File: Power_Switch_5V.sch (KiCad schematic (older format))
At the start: 7 parts

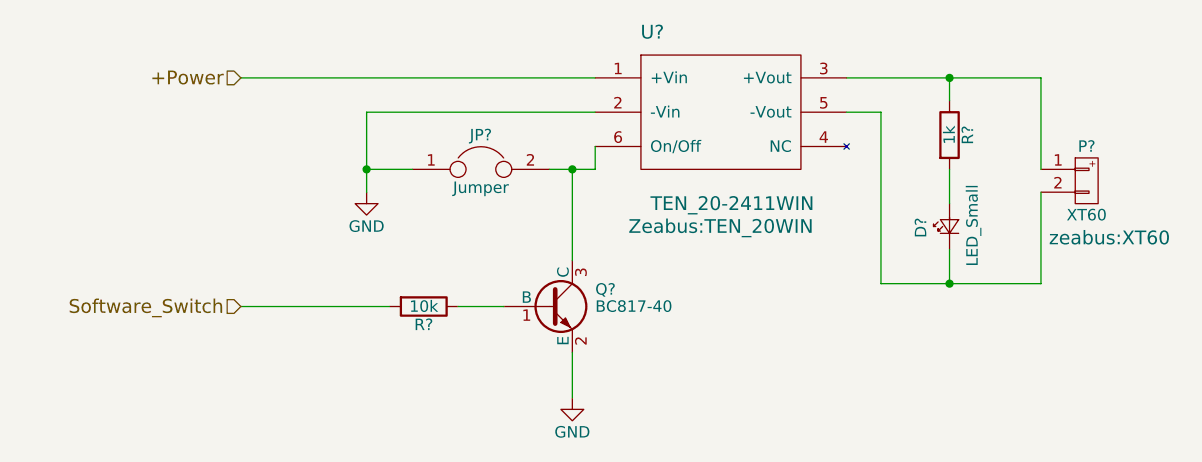
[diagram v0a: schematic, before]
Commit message: Annotate all components
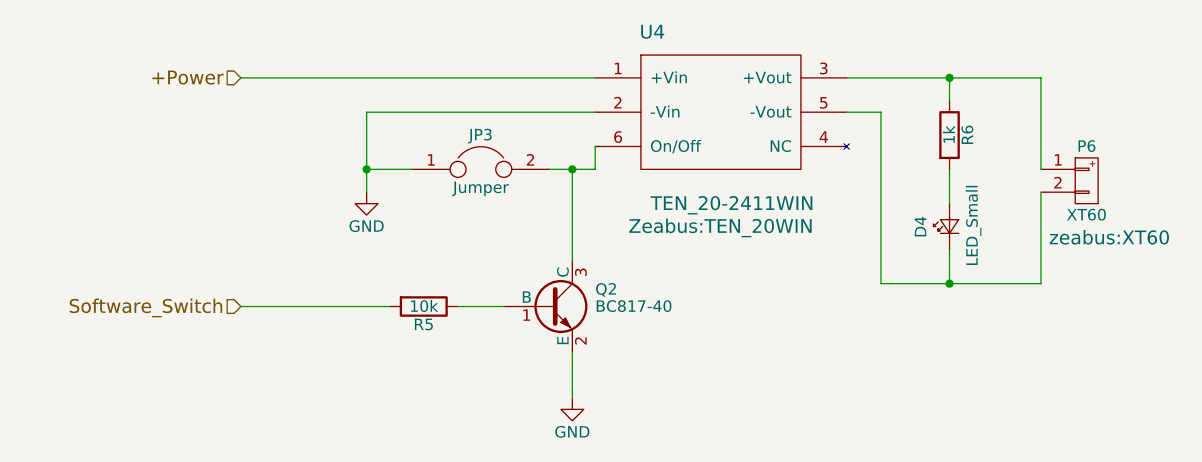
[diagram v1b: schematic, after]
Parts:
- gave numbers to parts that had none: 7
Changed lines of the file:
@@
 LIBS:zeabus
 LIBS:ftdi
-LIBS:Power_Distributor-cache
 EELAYER 25 0
 EELAYER END
@@
 $EndDescr
 $Comp
-L TEN_20-2411WIN U?
+L TEN_20-2411WIN U4
 U 1 1 58DFD91D
 P 5450 3700
-F 0 "U?" H 5150 4050 60  0000 C CNN
+F 0 "U4" H 5150 4050 60  0000 C CNN
 F 1 "TEN_20-2411WIN" H 5500 3300 60  0000 C CNN
 F 2 "Zeabus:TEN_20WIN" H 5450 3200 60  0000 C CNN
@@
 $EndComp
 $Comp
-L R R?
+L R R6
 U 1 1 58DFD99A
 P 6450 3800
-F 0 "R?" V 6530 3800 50  0000 C CNN
+F 0 "R6" V 6530 3800 50  0000 C CNN
 F 1 "1k" V 6450 3800 50  0000 C CNN
 F 2 "Resistors_SMD:R_0603" V 6380 3800 50  0001 C CNN
@@
 $EndComp
 $Comp
-L LED_Small D?
+L LED_Small D4
 U 1 1 58DFD9EF
 P 6450 4200
-F 0 "D?" H 6400 4325 50  0000 L CNN
+F 0 "D4" H 6400 4325 50  0000 L CNN
 F 1 "LED_Small" H 6275 4100 50  0000 L CNN
 F 2 "LEDs:LED_0603" V 6450 4200 50  0001 C CNN
@@
 $EndComp
 $Comp
-L XT60 P?
+L XT60 P6
 U 1 1 58DFDA4A
 P 7050 4000
-F 0 "P?" H 7050 4150 50  0000 C CNN
+F 0 "P6" H 7050 4150 50  0000 C CNN
 F 1 "XT60" H 7050 3850 50  0000 C CNN
 F 2 "zeabus:XT60" H 7150 3750 60  0000 C CNN
@@
 $EndComp
 $Comp
-L GND #PWR?
+L GND #PWR017
 U 1 1 58DFDAC1
 P 3900 4050
-F 0 "#PWR?" H 3900 3800 50  0001 C CNN
+F 0 "#PWR017" H 3900 3800 50  0001 C CNN
 F 1 "GND" H 3900 3900 50  0000 C CNN
 F 2 "" H 3900 4050 50  0001 C CNN
@@
 $EndComp
 $Comp
-L GND #PWR?
+L GND #PWR018
 U 1 1 58DFDADD
 P 4800 4950
-F 0 "#PWR?" H 4800 4700 50  0001 C CNN
+F 0 "#PWR018" H 4800 4700 50  0001 C CNN
 F 1 "GND" H 4800 4800 50  0000 C CNN
 F 2 "" H 4800 4950 50  0001 C CNN
@@
 $EndComp
 $Comp
-L Jumper JP?
+L Jumper JP3
 U 1 1 58DFDAF9
 P 4400 3950
-F 0 "JP?" H 4400 4100 50  0000 C CNN
+F 0 "JP3" H 4400 4100 50  0000 C CNN
 F 1 "Jumper" H 4400 3870 50  0000 C CNN
 F 2 "Pin_Headers:Pin_Header_Straight_1x02_Pitch2.00mm" H 4400 3950 50  0001 C CNN
@@
 Software_Switch
 $Comp
-L R R?
+L R R5
 U 1 1 58E00964
 P 4150 4550
-F 0 "R?" V 4230 4550 50  0000 C CNN
+F 0 "R5" V 4230 4550 50  0000 C CNN
 F 1 "10k" V 4150 4550 50  0000 C CNN
 F 2 "Resistors_SMD:R_0603" V 4080 4550 50  0001 C CNN
@@
 $EndComp
 $Comp
-L BC817-40 Q?
+L BC817-40 Q2
 U 1 1 58E56AD9
 P 4700 4550
-F 0 "Q?" H 4900 4625 50  0000 L CNN
+F 0 "Q2" H 4900 4625 50  0000 L CNN
 F 1 "BC817-40" H 4900 4550 50  0000 L CNN
 F 2 "TO_SOT_Packages_SMD:SOT-23" H 4900 4475 50  0001 L CIN
